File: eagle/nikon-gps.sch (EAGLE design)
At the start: 8 parts, among them IC1 GPS-A2235-H, IC2 LP2985SOT, IC3 MAX3370

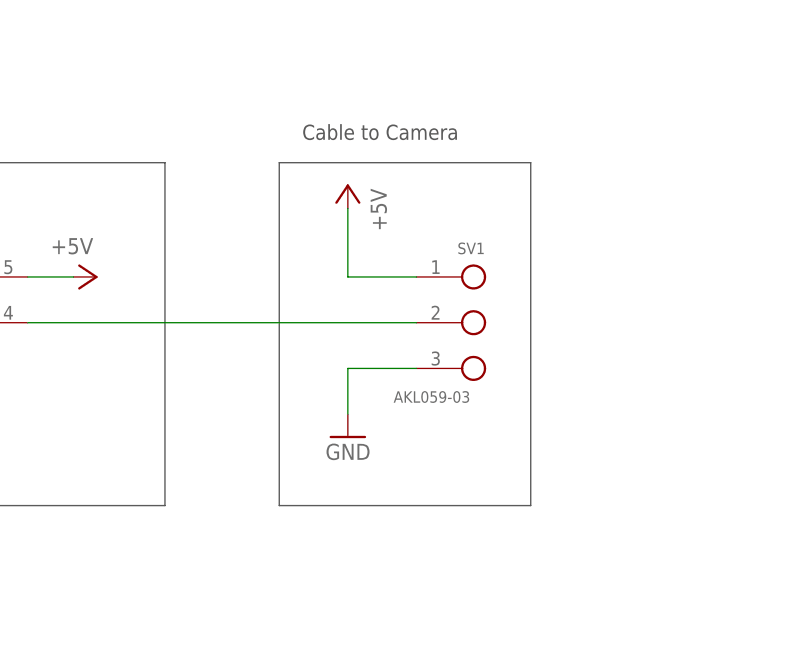
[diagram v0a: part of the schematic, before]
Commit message: First stab at a PCB layout.
The part placement might still be optimized, esp. if we consider adding
a Status-LED.
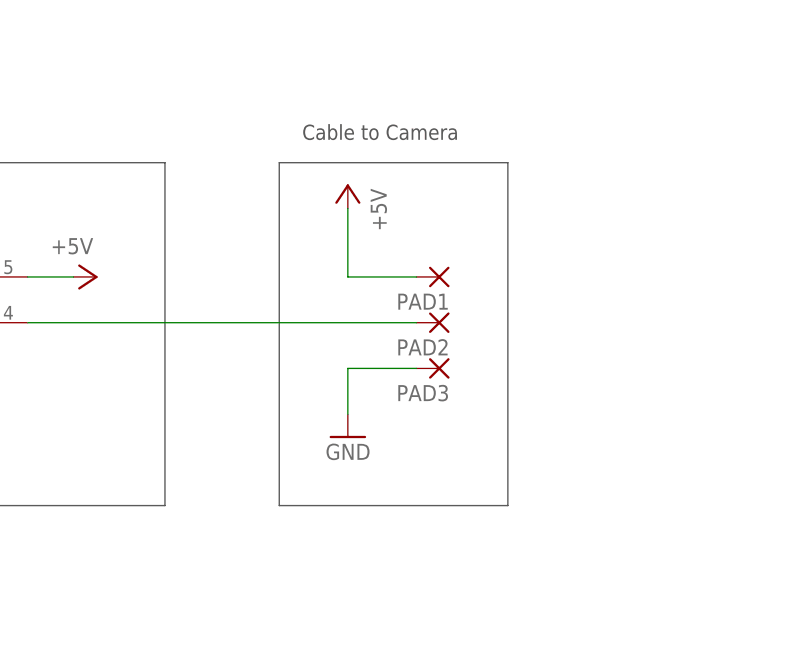
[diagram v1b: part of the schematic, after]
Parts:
- removed SV1: AKL059-03, selfmade:AKL059-03
- added PAD1, PAD2, PAD3: (no value), wirepad:SMD2
- C1: device rcl:C-EUC1206 -> rcl:C-EUC0805
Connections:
- net +5V: now also PAD1.P; no longer SV1.1
- net GND: now also PAD3.P; no longer SV1.3
- net N$3: now also PAD2.P; no longer SV1.2
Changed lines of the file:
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@@
 <grid distance="0.1" unitdist="inch" unit="inch" style="lines" multiple="1" display="no" altdistance="0.01" altunitdist="inch" altunit="inch"/>
 <layers>
-<layer number="1" name="Top" color="4" fill="1" visible="no" active="no"/>
-<layer number="16" name="Bottom" color="1" fill="1" visible="no" active="no"/>
-<layer number="17" name="Pads" color="2" fill="1" visible="no" active="no"/>
-<layer number="18" name="Vias" color="2" fill="1" visible="no" active="no"/>
-<layer number="19" name="Unrouted" color="6" fill="1" visible="no" active="no"/>
-<layer number="20" name="Dimension" color="15" fill="1" visible="no" active="no"/>
-<layer number="21" name="tPlace" color="7" fill="1" visible="no" active="no"/>
-<layer number="22" name="bPlace" color="7" fill="1" visible="no" active="no"/>
-<layer number="23" name="tOrigins" color="15" fill="1" visible="no" active="no"/>
-<layer number="24" name="bOrigins" color="15" fill="1" visible="no" active="no"/>
-<layer number="25" name="tNames" color="7" fill="1" visible="no" active="no"/>
-<layer number="26" name="bNames" color="7" fill="1" visible="no" active="no"/>
-<layer number="27" name="tValues" color="7" fill="1" visible="no" active="no"/>
-<layer number="28" name="bValues" color="7" fill="1" visible="no" active="no"/>
+<layer number="1" name="Top" color="4" fill="1" visible="yes" active="no"/>
+<layer number="16" name="Bottom" color="1" fill="1" visible="yes" active="no"/>
+<layer number="17" name="Pads" color="2" fill="1" visible="yes" active="no"/>
+<layer number="18" name="Vias" color="2" fill="1" visible="yes" active="no"/>
+<layer number="19" name="Unrouted" color="6" fill="1" visible="yes" active="no"/>
+<layer number="20" name="Dimension" color="15" fill="1" visible="yes" active="no"/>
+<layer number="21" name="tPlace" color="7" fill="1" visible="yes" active="no"/>
+<layer number="22" name="bPlace" color="7" fill="1" visible="yes" active="no"/>
+<layer number="23" name="tOrigins" color="15" fill="1" visible="yes" active="no"/>
+<layer number="24" name="bOrigins" color="15" fill="1" visible="yes" active="no"/>
+<layer number="25" name="tNames" color="7" fill="1" visible="yes" active="no"/>
+<layer number="26" name="bNames" color="7" fill="1" visible="yes" active="no"/>
+<layer number="27" name="tValues" color="7" fill="1" visible="yes" active="no"/>
+<layer number="28" name="bValues" color="7" fill="1" visible="yes" active="no"/>
 <layer number="29" name="tStop" color="7" fill="3" visible="no" active="no"/>
 <layer number="30" name="bStop" color="7" fill="6" visible="no" active="no"/>
@@
 <layer number="35" name="tGlue" color="7" fill="4" visible="no" active="no"/>
 <layer number="36" name="bGlue" color="7" fill="5" visible="no" active="no"/>
-<layer number="37" name="tTest" color="7" fill="1" visible="no" active="no"/>
-<layer number="38" name="bTest" color="7" fill="1" visible="no" active="no"/>
+<layer number="37" name="tTest" color="7" fill="1" visible="yes" active="no"/>
+<layer number="38" name="bTest" color="7" fill="1" visible="yes" active="no"/>
 <layer number="39" name="tKeepout" color="4" fill="11" visible="no" active="no"/>
 <layer number="40" name="bKeepout" color="1" fill="11" visible="no" active="no"/>
@@
 <layer number="44" name="Drills" color="7" fill="1" visible="no" active="no"/>
 <layer number="45" name="Holes" color="7" fill="1" visible="no" active="no"/>
-<layer number="46" name="Milling" color="3" fill="1" visible="no" active="no"/>
-<layer number="47" name="Measures" color="7" fill="1" visible="no" active="no"/>
-<layer number="48" name="Document" color="7" fill="1" visible="no" active="no"/>
-<layer number="49" name="Reference" color="7" fill="1" visible="no" active="no"/>
-<layer number="50" name="dxf" color="7" fill="1" visible="no" active="no"/>
-<layer number="51" name="tDocu" color="7" fill="1" visible="no" active="no"/>
-<layer number="52" name="bDocu" color="7" fill="1" visible="no" active="no"/>
+<layer number="46" name="Milling" color="3" fill="1" visible="yes" active="no"/>
+<layer number="47" name="Measures" color="7" fill="1" visible="yes" active="no"/>
+<layer number="48" name="Document" color="7" fill="1" visible="yes" active="no"/>
+<layer number="49" name="Reference" color="7" fill="1" visible="yes" active="no"/>
+<layer number="50" name="dxf" color="7" fill="1" visible="yes" active="no"/>
+<layer number="51" name="tDocu" color="7" fill="1" visible="yes" active="no"/>
+<layer number="52" name="bDocu" color="7" fill="1" visible="yes" active="no"/>
 <layer number="91" name="Nets" color="2" fill="1" visible="yes" active="yes"/>
 <layer number="92" name="Busses" color="1" fill="1" visible="yes" active="yes"/>
@@
 <part name="FRAME1" library="frames" deviceset="DINA4_L" device=""/>
 <part name="IC3" library="selfmade" deviceset="MAX3370" device=""/>
-<part name="SV1" library="selfmade" deviceset="AKL059-03" device=""/>
 <part name="GND1" library="supply1" deviceset="GND" device=""/>
 <part name="GND2" library="supply1" deviceset="GND" device=""/>
@@
 <part name="P+1" library="supply1" deviceset="+5V" device=""/>
 <part name="GND3" library="supply1" deviceset="GND" device=""/>
-<part name="C1" library="rcl" deviceset="C-EU" device="C1206" value="100n"/>
+<part name="C1" library="rcl" deviceset="C-EU" device="C0805" value="100n"/>
 <part name="GND4" library="supply1" deviceset="GND" device=""/>
 <part name="+3V2" library="supply1" deviceset="+3V3" device=""/>
@@
 <part name="R2" library="rcl" deviceset="R-EU_" device="M1206" value="2k2"/>
 <part name="R3" library="rcl" deviceset="R-EU_" device="M1206" value="2k2"/>
+<part name="PAD1" library="wirepad" deviceset="SMD2" device=""/>
+<part name="PAD2" library="wirepad" deviceset="SMD2" device=""/>
+<part name="PAD3" library="wirepad" deviceset="SMD2" device=""/>
 </parts>
 <sheets>
@@
 <wire x1="93.98" y1="15.24" x2="20.32" y2="15.24" width="0.1524" layer="97"/>
 <wire x1="20.32" y1="15.24" x2="20.32" y2="55.88" width="0.1524" layer="97"/>
-<wire x1="241.3" y1="147.32" x2="213.36" y2="147.32" width="0.1524" layer="97"/>
+<wire x1="238.76" y1="147.32" x2="213.36" y2="147.32" width="0.1524" layer="97"/>
 <wire x1="213.36" y1="147.32" x2="213.36" y2="109.22" width="0.1524" layer="97"/>
-<wire x1="213.36" y1="109.22" x2="241.3" y2="109.22" width="0.1524" layer="97"/>
-<wire x1="241.3" y1="109.22" x2="241.3" y2="147.32" width="0.1524" layer="97"/>
+<wire x1="213.36" y1="109.22" x2="238.76" y2="109.22" width="0.1524" layer="97"/>
+<wire x1="238.76" y1="109.22" x2="238.76" y2="147.32" width="0.1524" layer="97"/>
 <wire x1="200.66" y1="147.32" x2="129.54" y2="147.32" width="0.1524" layer="97"/>
 <wire x1="129.54" y1="147.32" x2="129.54" y2="109.22" width="0.1524" layer="97"/>
@@
 <instance part="FRAME1" gate="G$2" x="162.56" y="0"/>
 <instance part="IC3" gate="G$1" x="165.1" y="132.08"/>
-<instance part="SV1" gate="G$1" x="233.68" y="129.54" rot="MR0"/>
 <instance part="GND1" gate="1" x="220.98" y="116.84" rot="MR0"/>
 <instance part="GND2" gate="1" x="71.12" y="81.28"/>
@@
 <instance part="R2" gate="G$1" x="76.2" y="152.4"/>
 <instance part="R3" gate="G$1" x="76.2" y="144.78"/>
+<instance part="PAD1" gate="1" x="231.14" y="134.62" rot="R180"/>
+<instance part="PAD2" gate="1" x="231.14" y="129.54" rot="R180"/>
+<instance part="PAD3" gate="1" x="231.14" y="124.46" rot="R180"/>
 </instances>
 <busses>
@@
 <net name="GND" class="0">
 <segment>
-<pinref part="SV1" gate="G$1" pin="3"/>
 <pinref part="GND1" gate="1" pin="GND"/>
 <wire x1="228.6" y1="124.46" x2="220.98" y2="124.46" width="0.1524" layer="91"/>
 <wire x1="220.98" y1="124.46" x2="220.98" y2="119.38" width="0.1524" layer="91"/>
+<pinref part="PAD3" gate="1" pin="P"/>
 </segment>
 <segment>
@@
 <net name="+5V" class="0">
 <segment>
-<pinref part="SV1" gate="G$1" pin="1"/>
 <pinref part="P+3" gate="1" pin="+5V"/>
 <wire x1="228.6" y1="134.62" x2="220.98" y2="134.62" width="0.1524" layer="91"/>
 <wire x1="220.98" y1="134.62" x2="220.98" y2="142.24" width="0.1524" layer="91"/>
+<pinref part="PAD1" gate="1" pin="P"/>
 </segment>
 <segment>
@@
 <pinref part="IC3" gate="G$1" pin="I/O_VCC"/>
 <wire x1="185.42" y1="129.54" x2="228.6" y2="129.54" width="0.1524" layer="91"/>
-<pinref part="SV1" gate="G$1" pin="2"/>
-</segment>
-</net>
+<pinref part="PAD2" gate="1" pin="P"/>
+</segment>
+</net>

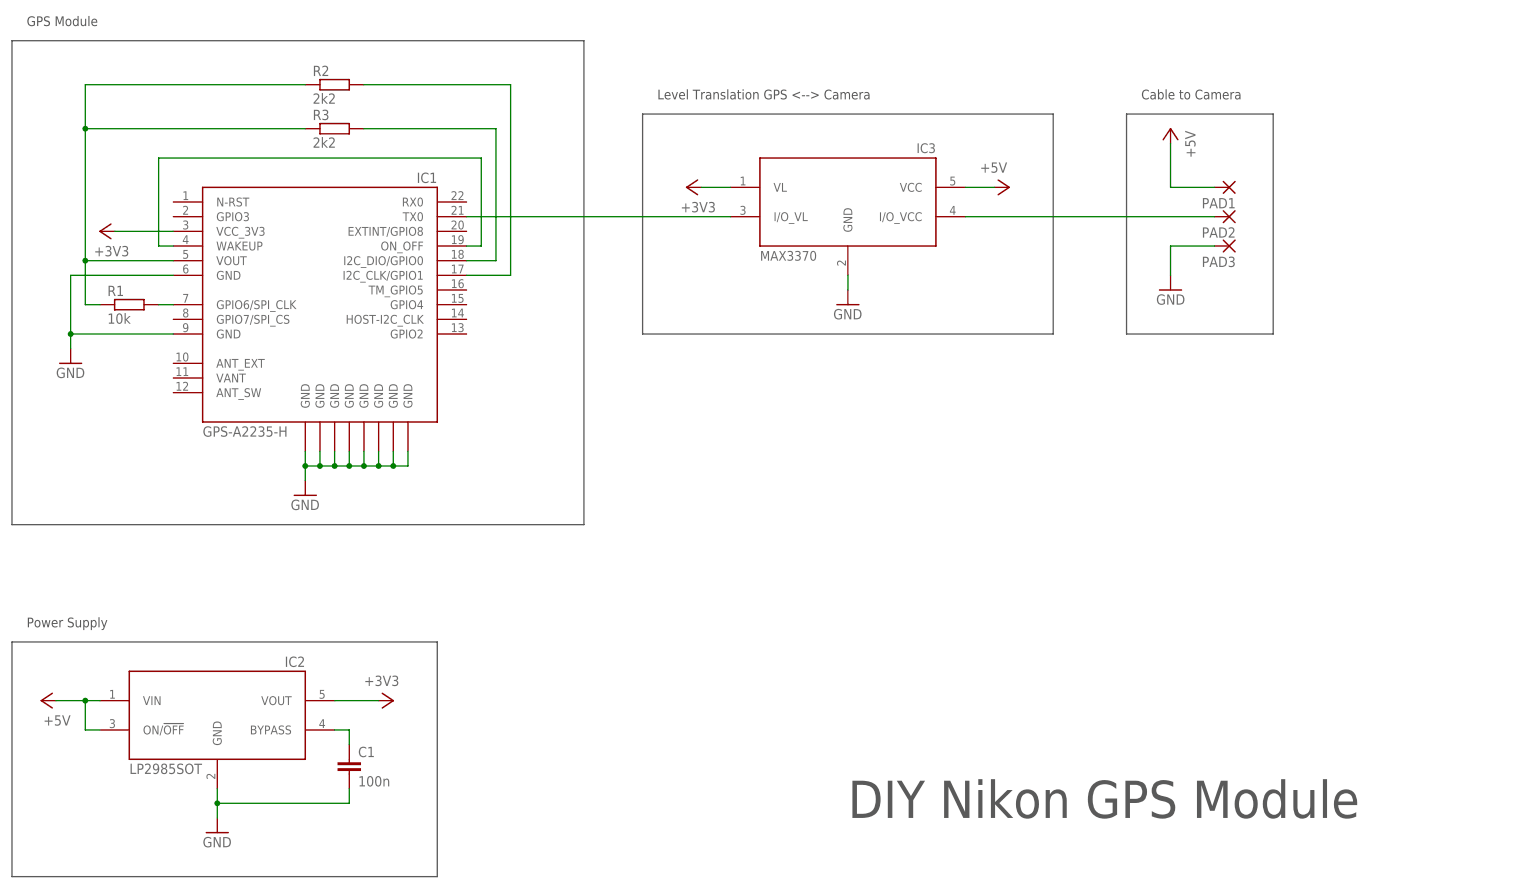
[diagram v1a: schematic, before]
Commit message: Adding missing capacitors for LP2985 voltage regulator.
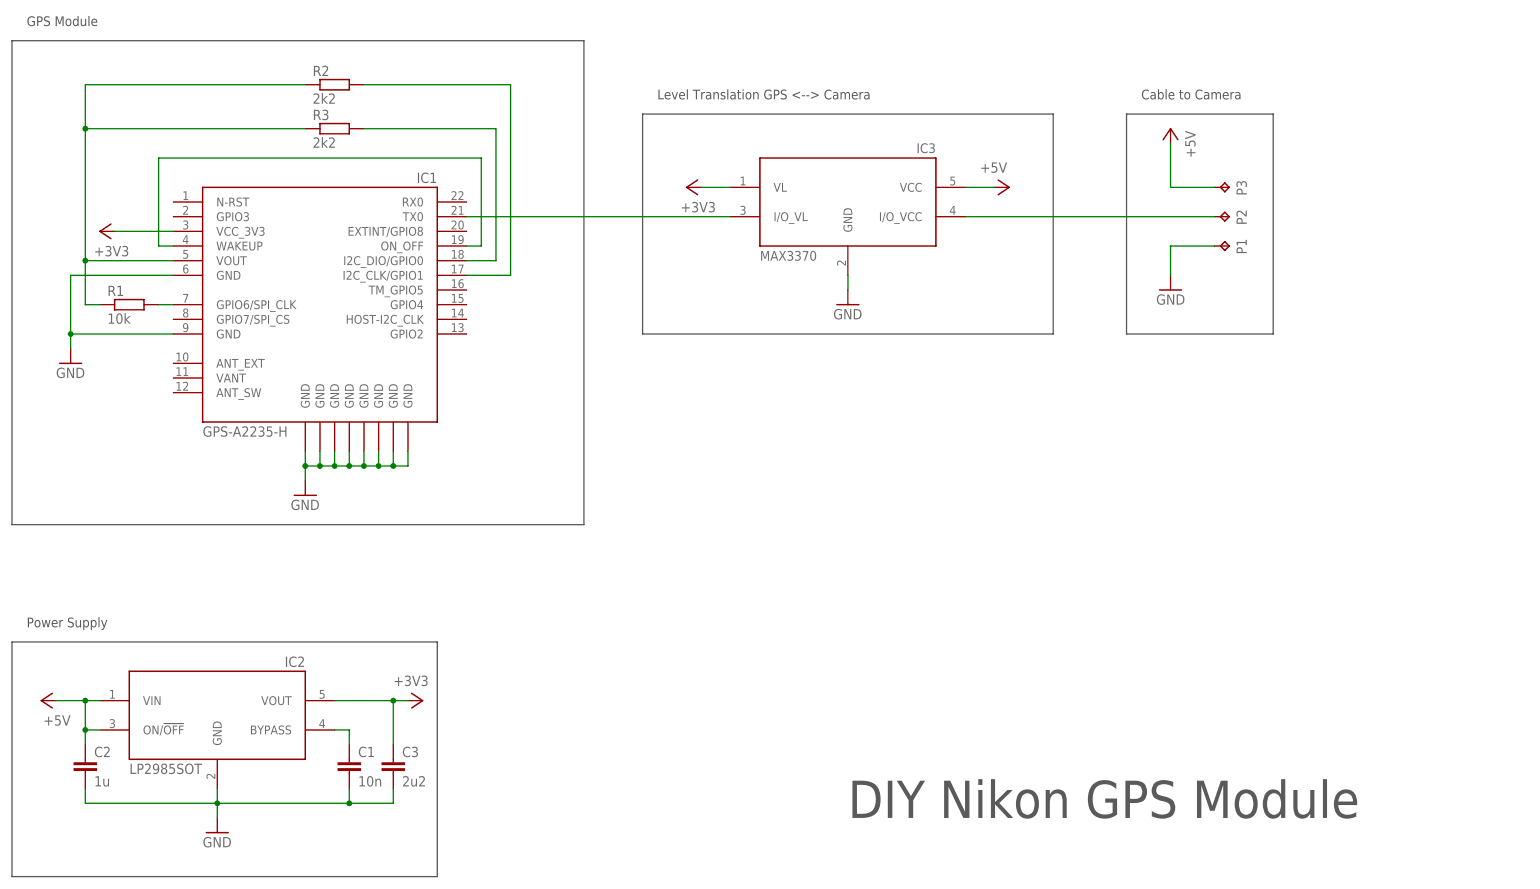
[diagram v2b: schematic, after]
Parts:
- removed PAD1, PAD2, PAD3: (no value), wirepad:SMD2
- added C2: 1u, rcl:C-EUC0805
- added C3: 2u2, rcl:C-EUC0805
- added P1, P2, P3: TPTP12SQ, testpad:TPTP12SQ
- C1: value 100n -> 10n
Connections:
- net +3V3: now also C3.1
- net +5V: now also C2.1, P3.TP; no longer PAD1.P
- net GND: now also C2.2, C3.2, P1.TP; no longer PAD3.P
- net N$3: now also P2.TP; no longer PAD2.P
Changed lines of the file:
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@@
 <part name="P+1" library="supply1" deviceset="+5V" device=""/>
 <part name="GND3" library="supply1" deviceset="GND" device=""/>
-<part name="C1" library="rcl" deviceset="C-EU" device="C0805" value="100n"/>
+<part name="C1" library="rcl" deviceset="C-EU" device="C0805" value="10n"/>
 <part name="GND4" library="supply1" deviceset="GND" device=""/>
 <part name="+3V2" library="supply1" deviceset="+3V3" device=""/>
@@
 <part name="R2" library="rcl" deviceset="R-EU_" device="M1206" value="2k2"/>
 <part name="R3" library="rcl" deviceset="R-EU_" device="M1206" value="2k2"/>
-<part name="PAD1" library="wirepad" deviceset="SMD2" device=""/>
-<part name="PAD2" library="wirepad" deviceset="SMD2" device=""/>
-<part name="PAD3" library="wirepad" deviceset="SMD2" device=""/>
+<part name="C2" library="rcl" deviceset="C-EU" device="C0805" value="1u"/>
+<part name="C3" library="rcl" deviceset="C-EU" device="C0805" value="2u2"/>
+<part name="P3" library="testpad" deviceset="TP" device="TP12SQ" value="TPTP12SQ"/>
+<part name="P2" library="testpad" deviceset="TP" device="TP12SQ" value="TPTP12SQ"/>
+<part name="P1" library="testpad" deviceset="TP" device="TP12SQ" value="TPTP12SQ"/>
 </parts>
 <sheets>
@@
 <instance part="GND1" gate="1" x="220.98" y="116.84" rot="MR0"/>
 <instance part="GND2" gate="1" x="71.12" y="81.28"/>
-<instance part="+3V1" gate="G$1" x="86.36" y="45.72" rot="R270"/>
+<instance part="+3V1" gate="G$1" x="91.44" y="45.72" rot="R270"/>
 <instance part="P+3" gate="1" x="220.98" y="144.78" rot="MR0"/>
 <instance part="P+1" gate="1" x="25.4" y="45.72" rot="R90"/>
@@
 <instance part="R2" gate="G$1" x="76.2" y="152.4"/>
 <instance part="R3" gate="G$1" x="76.2" y="144.78"/>
-<instance part="PAD1" gate="1" x="231.14" y="134.62" rot="R180"/>
-<instance part="PAD2" gate="1" x="231.14" y="129.54" rot="R180"/>
-<instance part="PAD3" gate="1" x="231.14" y="124.46" rot="R180"/>
+<instance part="C2" gate="G$1" x="33.02" y="35.56"/>
+<instance part="C3" gate="G$1" x="86.36" y="35.56"/>
+<instance part="P3" gate="G$1" x="231.14" y="134.62" rot="R270"/>
+<instance part="P2" gate="G$1" x="231.14" y="129.54" rot="R270"/>
+<instance part="P1" gate="G$1" x="231.14" y="124.46" rot="R270"/>
 </instances>
 <busses>
@@
 <wire x1="228.6" y1="124.46" x2="220.98" y2="124.46" width="0.1524" layer="91"/>
 <wire x1="220.98" y1="124.46" x2="220.98" y2="119.38" width="0.1524" layer="91"/>
-<pinref part="PAD3" gate="1" pin="P"/>
+<pinref part="P1" gate="G$1" pin="TP"/>
 </segment>
 <segment>
@@
 <wire x1="78.74" y1="27.94" x2="78.74" y2="30.48" width="0.1524" layer="91"/>
 <junction x="55.88" y="27.94"/>
+<pinref part="C2" gate="G$1" pin="2"/>
+<wire x1="33.02" y1="30.48" x2="33.02" y2="27.94" width="0.1524" layer="91"/>
+<wire x1="33.02" y1="27.94" x2="55.88" y2="27.94" width="0.1524" layer="91"/>
+<pinref part="C3" gate="G$1" pin="2"/>
+<wire x1="78.74" y1="27.94" x2="86.36" y2="27.94" width="0.1524" layer="91"/>
+<wire x1="86.36" y1="27.94" x2="86.36" y2="30.48" width="0.1524" layer="91"/>
+<junction x="78.74" y="27.94"/>
 </segment>
 <segment>
@@
 <wire x1="228.6" y1="134.62" x2="220.98" y2="134.62" width="0.1524" layer="91"/>
 <wire x1="220.98" y1="134.62" x2="220.98" y2="142.24" width="0.1524" layer="91"/>
-<pinref part="PAD1" gate="1" pin="P"/>
+<pinref part="P3" gate="G$1" pin="TP"/>
 </segment>
 <segment>
@@
 <wire x1="33.02" y1="40.64" x2="35.56" y2="40.64" width="0.1524" layer="91"/>
 <junction x="33.02" y="45.72"/>
+<pinref part="C2" gate="G$1" pin="1"/>
+<wire x1="33.02" y1="40.64" x2="33.02" y2="38.1" width="0.1524" layer="91"/>
+<junction x="33.02" y="40.64"/>
 </segment>
 <segment>
@@
 <pinref part="IC2" gate="G$1" pin="VOUT"/>
 <pinref part="+3V1" gate="G$1" pin="+3V3"/>
-<wire x1="76.2" y1="45.72" x2="83.82" y2="45.72" width="0.1524" layer="91"/>
+<wire x1="76.2" y1="45.72" x2="86.36" y2="45.72" width="0.1524" layer="91"/>
+<pinref part="C3" gate="G$1" pin="1"/>
+<wire x1="86.36" y1="45.72" x2="88.9" y2="45.72" width="0.1524" layer="91"/>
+<wire x1="86.36" y1="38.1" x2="86.36" y2="45.72" width="0.1524" layer="91"/>
+<junction x="86.36" y="45.72"/>
 </segment>
 <segment>
@@
 <pinref part="IC3" gate="G$1" pin="I/O_VCC"/>
 <wire x1="185.42" y1="129.54" x2="228.6" y2="129.54" width="0.1524" layer="91"/>
-<pinref part="PAD2" gate="1" pin="P"/>
-</segment>
-</net>
+<pinref part="P2" gate="G$1" pin="TP"/>
+</segment>
+</net>
